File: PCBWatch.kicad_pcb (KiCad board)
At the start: 2 copper layers, 45 x 73.2 mm, 45 parts, among them J1 UART Pads, J2 E-Ink connector, J3 Pin header A, J4 Pin header B, J6 Pin header A top, J7 Pin header B top, Q1 Si1304BDL / Si1308EDL TUBE MOS, U1 STM32L010C6Tx, Y1 32.768KHZ

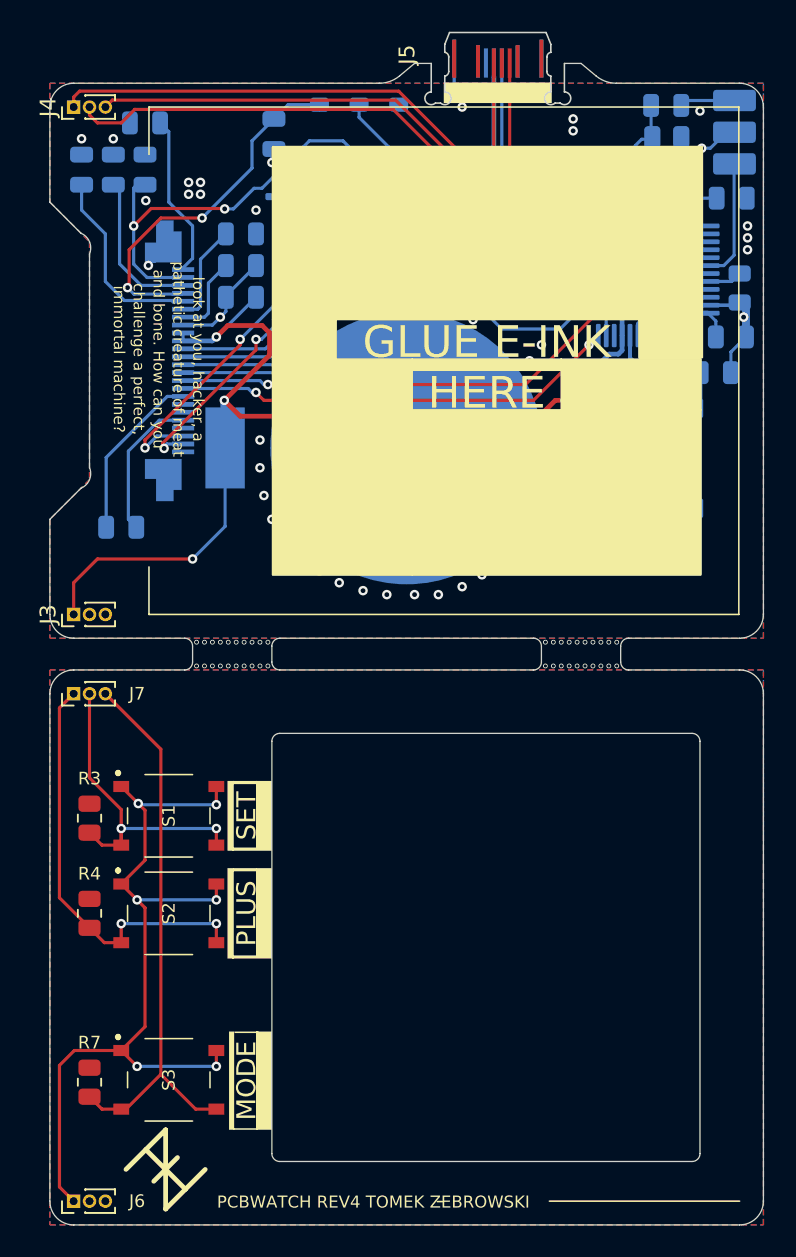
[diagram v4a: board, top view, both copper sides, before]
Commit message: Fix fpc pin ordering
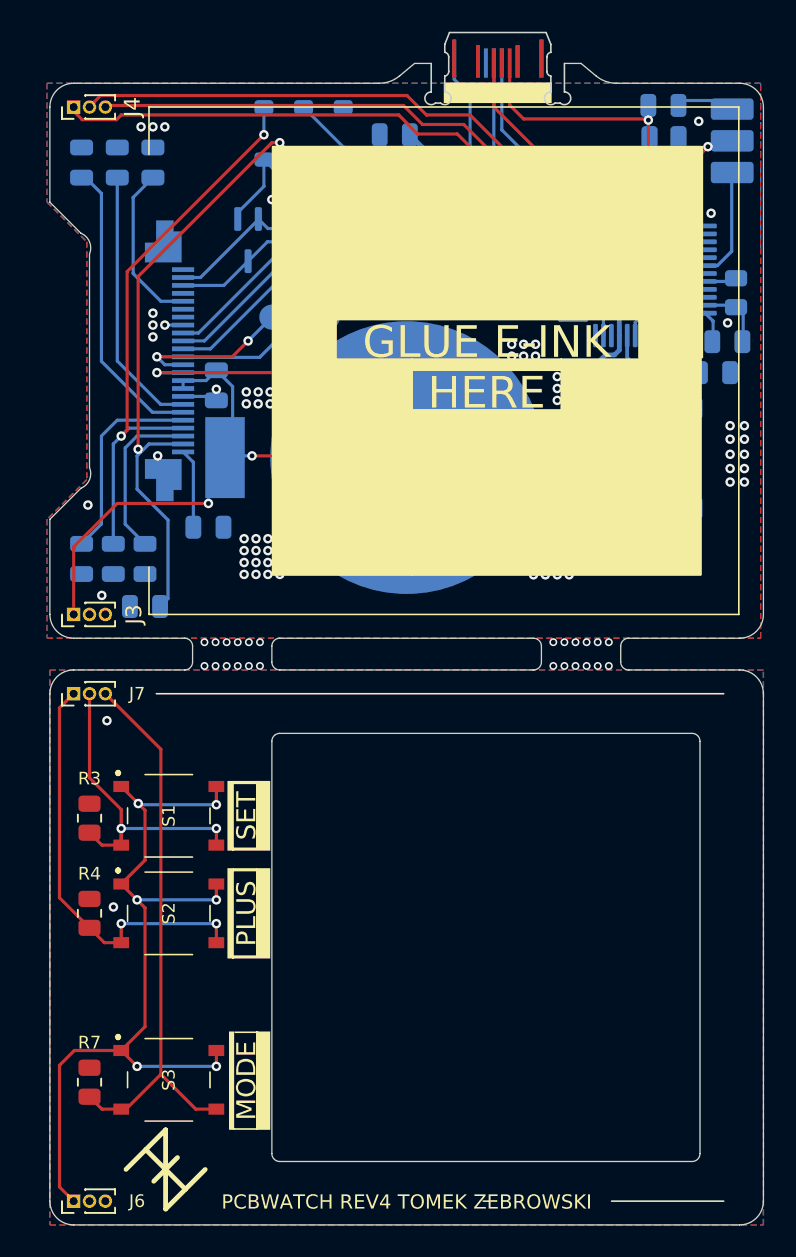
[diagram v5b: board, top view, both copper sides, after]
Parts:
- moved C11 28.7 mm to (204.0, 55.0)
- moved C18 27.6 mm to (206.0, 58.0), turned to 180 degrees
- moved C16 25.8 mm to (210.0, 53.0), turned to 0 degrees
- moved C15 24.6 mm to (206.0, 55.0), turned to -90 degrees
- moved C14 24.6 mm to (202.0, 55.0), turned to -90 degrees
- moved C19 23.1 mm to (206.5, 30.0), turned to 90 degrees
- moved C4 14.2 mm to (228.8, 33.2), turned to -90 degrees
- moved C17 11.0 mm to (202.0, 30.0), turned to 90 degrees
- moved C13 10.2 mm to (204.2, 30.0), turned to 90 degrees
- moved C9 7.59 mm to (221.8, 28.2), turned to 180 degrees
- moved C12 5.76 mm to (210.5, 44.0), turned to -90 degrees
- moved Q1 4.19 mm to (212.5, 34.9), turned to -90 degrees
- moved R6 3.90 mm to (217.0, 33.2), turned to -90 degrees
- moved C10 3.75 mm to (221.8, 30.2), turned to 0 degrees
- moved D1 3.50 mm to (216.0, 28.2)
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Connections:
- U1 pad 11: /RES -> /BUTTON3
- U1 pad 12: /BUSY -> unconnected-(U1-PA2-Pad12)
- U1 pad 13: /D/C -> unconnected-(U1-PA3-Pad13)
- U1 pad 18: unconnected-(U1-PB0-Pad18) -> /D/C
- U1 pad 19: unconnected-(U1-PB1-Pad19) -> /RES
- U1 pad 20: /BUTTON1 -> /BUSY
- U1 pad 21: /BUTTON3 -> /BUTTON2
- U1 pad 22: /BUTTON2 -> /BUTTON1
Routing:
- net GND: track 47.0 -> 31.9 mm, vias 53 -> 89
- net /GDR: track 21.6 -> 8.40 mm, vias 2 -> 0
- net /PREVGL: track 25.8 -> 39.0 mm
- net /RESE: track 22.7 -> 10.1 mm, vias 2 -> 0
- net /PREVGH: track 23.1 -> 35.6 mm
- net Net-(J2-VPP): track 6.41 -> 18.5 mm
- net Net-(J2-VDD): track 5.16 -> 16.8 mm
- net +3V0: track 125.1 -> 114.7 mm, vias 6 -> 5
- net Net-(D3-A): track 8.64 -> 16.4 mm
- net /SDI: track 27.8 -> 34.1 mm, vias 0 -> 2
- net /BUTTON1: track 39.1 -> 44.5 mm
- net Net-(J2-VCOM): track 10.3 -> 5.02 mm
- net /BUTTON3: track 35.1 -> 40.4 mm
- net /SWDIO: track 19.1 -> 15.9 mm
- net /SCLK: track 27.0 -> 30.3 mm, vias 0 -> 2
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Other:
- board text added: "2032"
- board text added: "can you challenge a perfect,"
- board text added: "creature of meat and bone. How"
- board text added: "look at you, hacker, a pathetic"
- board text removed: "CR2032 3V"
- board text removed: "CS"
- board text removed: "and bone. How can you"
- board text removed: "challenge a perfect,"
- board text removed: "look at you, hacker, a"
- board text removed: "pathetic creature of meat"

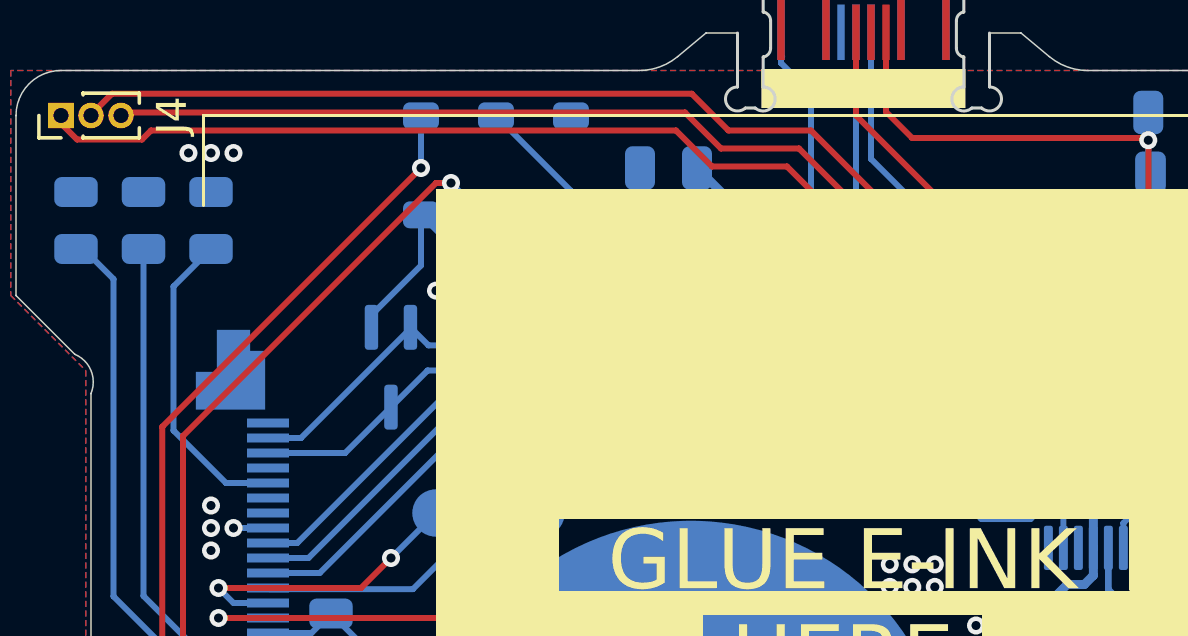
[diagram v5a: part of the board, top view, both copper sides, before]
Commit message: Add prevgh prevgl testpoints
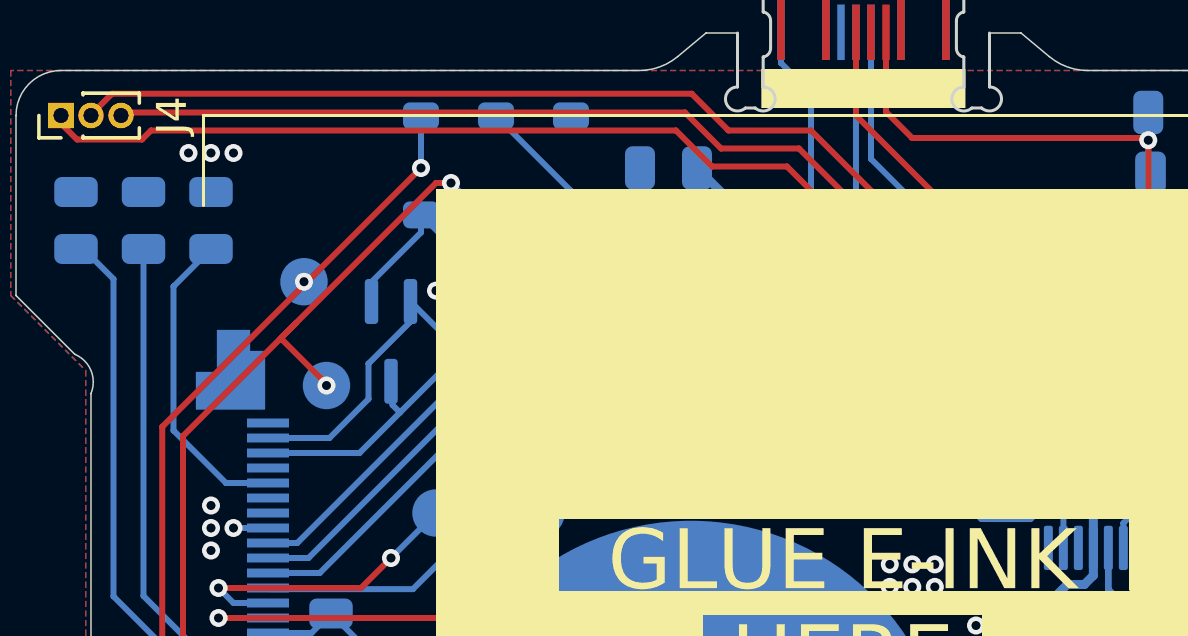
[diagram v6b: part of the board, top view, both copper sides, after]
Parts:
- moved Q1 0.86 mm to (212.5, 34.0)
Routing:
- net /PREVGL: track 39.0 -> 41.9 mm, vias 2 -> 3
- net /GDR: track 8.40 -> 10.2 mm
- net Net-(D3-A): track 16.4 -> 14.9 mm
- net /RESE: track 10.1 -> 11.3 mm
- net /PREVGH: vias 2 -> 3
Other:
- board text added: "PGH"
- board text added: "PGL"
